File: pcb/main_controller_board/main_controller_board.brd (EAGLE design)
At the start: 72.1 x 52.1 mm, 3 parts, among them U1 RPI_CAMERA, U2 RPI_CAMERA

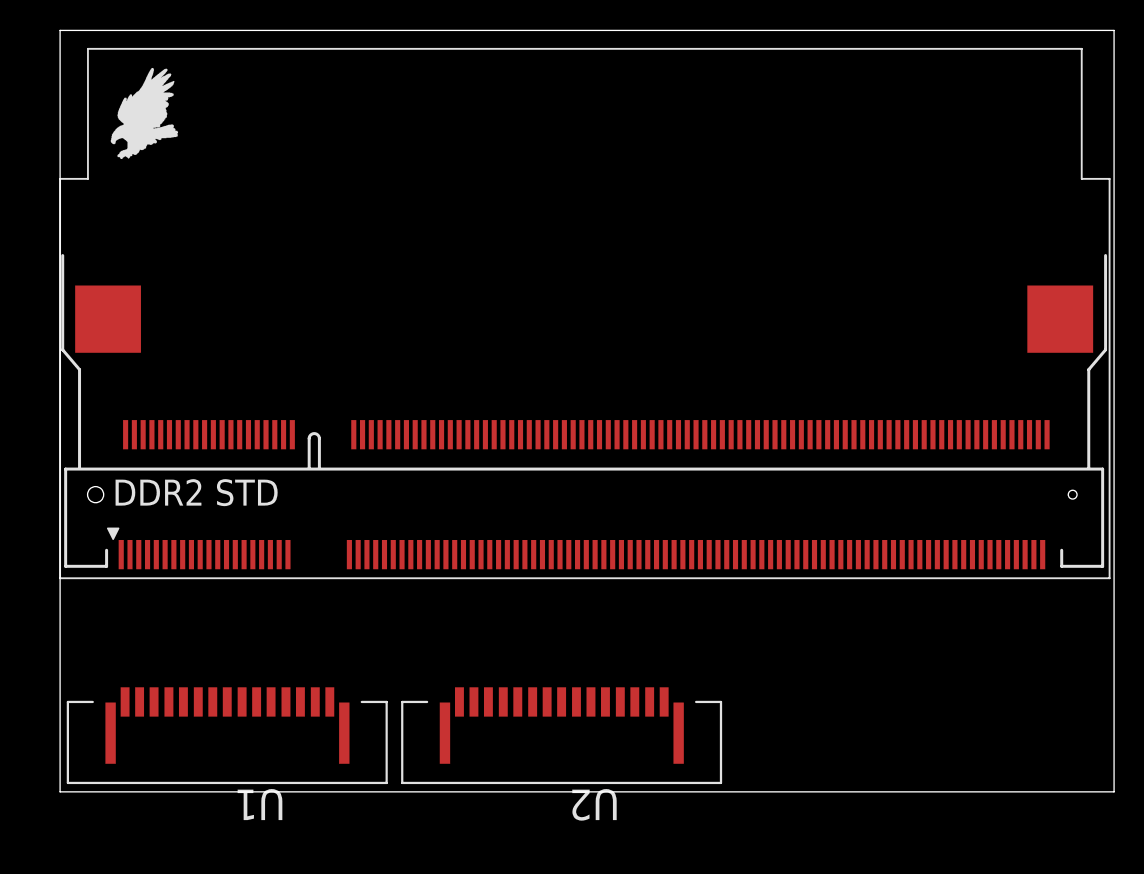
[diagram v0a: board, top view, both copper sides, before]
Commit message: add dc-dc
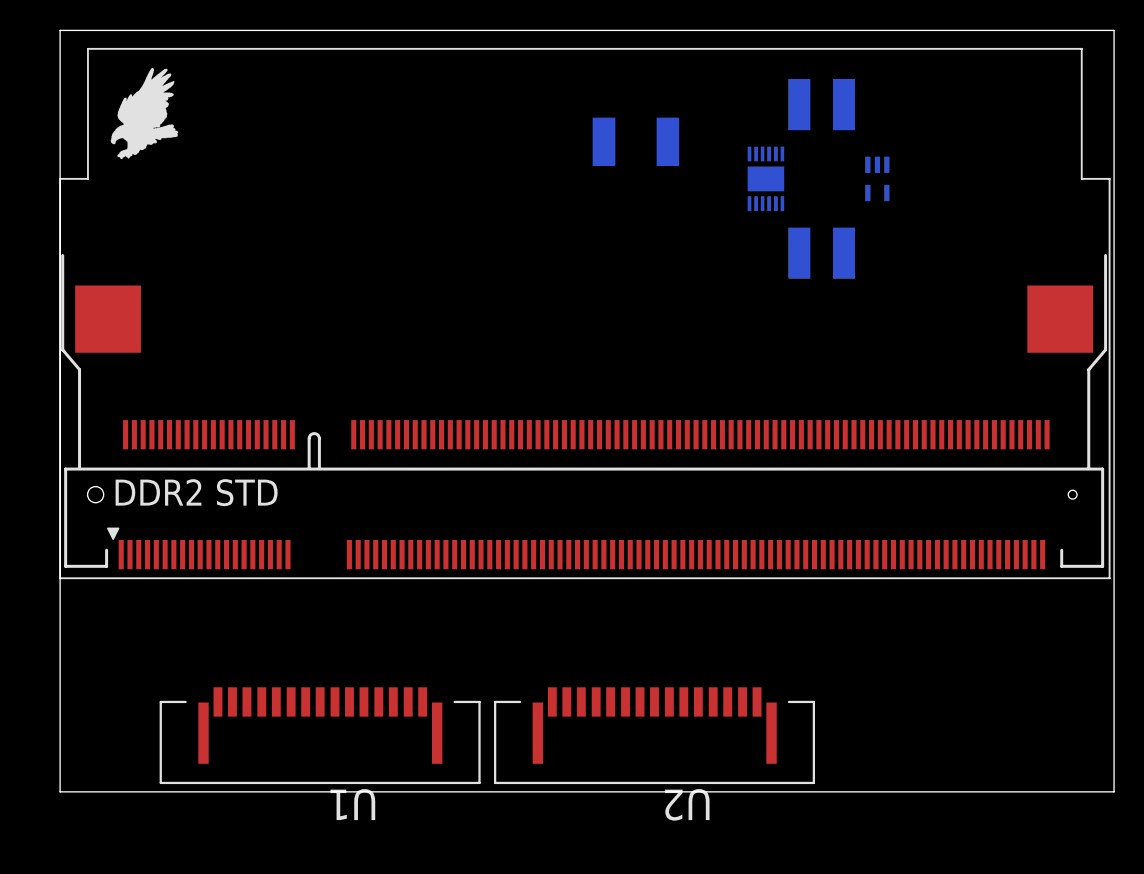
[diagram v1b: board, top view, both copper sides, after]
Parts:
- added F1: (no value), openblw:1812
- added L1, L2: (no value), openblw:BOURNS-SRN4018
- added U$1: PAM2306, openblw:WDFN3X3-12L
- added U$2: AP7115-XXSEG, openblw:SOT353
- moved U1 6.35 mm to (17.8, 8.89)
- moved U2 6.35 mm to (40.6, 8.89)
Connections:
- new net IN: U$2.1

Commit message: porovisional wiring
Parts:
- added C1, C9: 100n, resistor:C0402
- added C10: 4.7u, resistor:C0603
- added C11, C12, C13, C14: (no value), resistor:C1206
- added C2, C3, C6, C7: 10u, resistor:C0805
- added C4, C5: NF, resistor:C0402
- added C8: 1u, resistor:C0402
- added CN1: (no value), openblw:JST-PH-2-THM
- added H1, H2, H3, H4: MOUNT-PAD-ROUND2.8, holes:2,8-PAD
- added IC1: (no value), openblw:DIP_3PIN
- added JP1: (no value), pinhead:1X04
- added K1: 61400416021, openblw:61400416021
- added LED1: RED, led:CHIP-LED0603
- added LED2: GREEN, led:CHIP-LED0603
- added R1, R11, R12: 100K, resistor:R0402
- added R10, R7, R8, R9: 0R, resistor:R0805
- added R13, R14, R16, R17: 1.8K, resistor:R0402
- added R15, R6: 470R, resistor:R0402
- added R2, R3: 0R, resistor:R0402
- added R4, R5: NR, resistor:R0402
- added U$3: DMG1012T, openblw:SOT523
- F1: value (none) -> MF-MSMF110/16
- L1, L2: value (none) -> 4.7u
- moved U$2 44.7 mm to (11.2, 40.6), turned to 0 degrees
- moved L1 35.3 mm to (16.8, 48.0), turned to 180 degrees
- moved U1 30.7 mm to (48.5, 8.26)
- moved U$1 27.5 mm to (20.8, 42.9)
- moved L2 27.2 mm to (24.9, 37.8)
- moved U2 18.9 mm to (21.7, 8.26)
- moved F1 12.8 mm to (52.1, 43.2), flipped to the top, turned to 270 degrees
- moved PCB1 1.42 mm to (36.2, 21.6), flipped to the bottom
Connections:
- removed net IN: U$2.1
- new net +12V: F1.2, IC1.IN
- new net +1V8: C5.1, C7.1, L2.P$1, R3.1, R9.2
- new net +2V5: C10.1, R10.2, U$2.5
- new net +3V3: C4.1, C6.1, C8.1, L1.P$1, R13.2, R14.2, R15.1, R16.2, R17.2, R2.1, R6.1, R7.2, R8.2, U$2.1, U$2.3, U1.15, U2.15
- new net +5V: C11.1, C2.1, C3.1, IC1.OUT, JP1.1, K1.1, R1.1, U$1.1, U$1.6, U$1.7
- new net BOTTOM_LIGHT_ENABLED: PCB1.59
- new net CAM0_CN: PCB1.144, U1.8
- new net CAM0_CP: PCB1.142, U1.9
- new net CAM0_DN0: PCB1.138, U1.2
- new net CAM0_DN1: PCB1.150, U1.5
- new net CAM0_DP0: PCB1.136, U1.3
- new net CAM0_DP1: PCB1.148, U1.6
- new net CAM0_IO0: PCB1.36, U1.11
- new net CAM0_IO1: PCB1.34, U1.12
- new net CAM0_SCL: PCB1.30, R13.1, U1.13
- new net CAM0_SDA: PCB1.28, R14.1, U1.14
- new net CAM1_CN: PCB1.149, U2.8
- new net CAM1_CP: PCB1.147, U2.9
- new net CAM1_DN0: PCB1.161, U2.2
- new net CAM1_DN1: PCB1.155, U2.5
- new net CAM1_DP0: PCB1.159, U2.3
- new net CAM1_DP1: PCB1.153, U2.6
- new net CAM1_IO0: PCB1.11, U2.11
- new net CAM1_IO1: PCB1.9, U2.12
- new net CAM1_SCL: PCB1.5, R17.1, U2.13
- new net CAM1_SDA: PCB1.3, R16.1, U2.14
- new net CM_1V8: C12.1, PCB1.183, PCB1.184, PCB1.185, PCB1.186, R9.1
- new net CM_3V3: C13.1, PCB1.191, PCB1.192, PCB1.193, PCB1.194, R8.1
- new net CM_VBAT: C14.1, PCB1.197, PCB1.198, PCB1.199, PCB1.200, R7.1
- new net CM_VDAC: PCB1.189, PCB1.190, R10.1
- new net EMMC_DISABLE_N: PCB1.2
- new net EXT0: PCB1.63
- new net EXT1: PCB1.65
- new net GND: C1.2, C10.2, C11.2, C12.2, C13.2, C14.2, C2.2, C3.2, C6.2, C7.2, C8.2, C9.2, CN1.2, H1.B2,8, H2.B2,8, H3.B2,8, H4.B2,8, IC1.GND, JP1.4, K1.4, LED1.C, PCB1.1, PCB1.103, PCB1.104, PCB1.109, PCB1.110, PCB1.115, PCB1.121, PCB1.122, PCB1.127, PCB1.13, PCB1.133, PCB1.134, PCB1.139, PCB1.140, PCB1.145, PCB1.146, PCB1.151, PCB1.152, PCB1.157, PCB1.163, PCB1.164, PCB1.169, PCB1.170, PCB1.181, PCB1.182, PCB1.187, PCB1.188, PCB1.19, PCB1.195, PCB1.196, PCB1.25, PCB1.26, PCB1.31, PCB1.32, PCB1.37, PCB1.38, PCB1.43, PCB1.44, PCB1.49, PCB1.50, PCB1.55, PCB1.56, PCB1.61, PCB1.62, PCB1.67, PCB1.68, PCB1.7, PCB1.73, PCB1.74, PCB1.79, PCB1.80, PCB1.85, PCB1.86, PCB1.91, PCB1.92, PCB1.97, PCB1.98, R11.2, R12.2, R4.2, R5.2, U$1.3, U$1.9, U$1.PAD, U$2.2, U$3.2, U1.1, U1.10, U1.4, U1.7, U2.1, U2.10, U2.4, U2.7
- new net GPIO47_1V8: PCB1.90, U$3.1
- new net N$1: C1.1, R1.2, U$1.12
- new net N$10: C5.2, R3.2, R4.1, U$1.10
- new net N$11: PCB1.154
- new net N$12: PCB1.156
- new net N$13: PCB1.158
- new net N$14: PCB1.160
- new net N$15: PCB1.162
- new net N$16: PCB1.10
- new net N$17: PCB1.12
- new net N$18: PCB1.14
- new net N$19: PCB1.16
- new net N$2: L1.P$2, U$1.8
- new net N$20: PCB1.18
- new net N$21: PCB1.20
- new net N$22: PCB1.22
- new net N$23: PCB1.24
- new net N$24: PCB1.124
- new net N$25: PCB1.126
- new net N$26: PCB1.128
- new net N$27: PCB1.130
- new net N$28: PCB1.132
- new net N$29: PCB1.4
- new net N$3: U$1.5
- new net N$30: PCB1.6
- new net N$31: PCB1.82, R12.1
- new net N$32: LED2.A, R15.2
- new net N$33: LED2.C, U$3.3
- new net N$34: PCB1.84, R11.1
- new net N$35: PCB1.8
- new net N$4: U$1.11
- new net N$5: C9.1, U$2.4
- new net N$6: CN1.1, F1.1
- new net N$7: L2.P$2, U$1.2
- new net N$8: C4.2, R2.2, R5.1, U$1.4
- new net N$9: LED1.A, R6.2
- new net TOP_LIGHT_ENABLED: PCB1.57
- new net UART_RX: JP1.3, PCB1.53
- new net UART_TX: JP1.2, PCB1.51
- new net USB_DN: K1.2, PCB1.167
- new net USB_DP: K1.3, PCB1.165
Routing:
- net +3V3: track 0.00 -> 185.0 mm, vias 0 -> 6
- net +5V: track 0.00 -> 72.1 mm, vias 0 -> 2
- net CAM1_SDA: track 0.00 -> 50.6 mm, vias 0 -> 1
- net CAM1_SCL: track 0.00 -> 47.3 mm, vias 0 -> 1
- net CAM1_IO0: track 0.00 -> 47.0 mm, vias 0 -> 1
- net CAM1_IO1: track 0.00 -> 46.8 mm, vias 0 -> 1
- net CAM0_CP: track 0.00 -> 43.5 mm, vias 0 -> 1
- net CAM0_CN: track 0.00 -> 42.7 mm, vias 0 -> 1
- net CAM0_DN1: track 0.00 -> 42.2 mm, vias 0 -> 1
- net CAM0_DP1: track 0.00 -> 42.1 mm, vias 0 -> 1
- net GPIO47_1V8: track 0.00 -> 40.7 mm, vias 0 -> 1
- net USB_DN: track 0.00 -> 36.2 mm, vias 0 -> 1
- net CAM0_DP0: track 0.00 -> 35.8 mm, vias 0 -> 1
- net CAM0_DN0: track 0.00 -> 35.5 mm, vias 0 -> 1
- net USB_DP: track 0.00 -> 35.3 mm, vias 0 -> 1
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- added copper zone on layer 16, net CM_1V8
- added copper zone on layer 16, net CM_3V3
- added copper zone on layer 16, net CM_VBAT
- added copper zone on layer 1, net GND
- added copper zone on layer 16, net GND

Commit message: rev0.1
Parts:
- added U$4: TENDA_P200, openblw:TENDA_P200
- moved JP1 40.1 mm to (22.9, 29.0), turned to 0 degrees
- moved R16 34.0 mm to (34.8, 4.06), flipped to the top, turned to 0 degrees
- moved R17 33.2 mm to (34.8, 2.79), flipped to the top, turned to 0 degrees
- moved C11 30.2 mm to (19.1, 35.6), turned to 180 degrees
- moved F1 27.0 mm to (25.1, 41.4)
- moved R13 26.6 mm to (61.5, 2.79), flipped to the top, turned to 0 degrees
- moved CN1 26.0 mm to (24.9, 46.7)
- moved IC1 25.8 mm to (25.1, 33.0)
- moved R14 25.2 mm to (61.5, 4.06), flipped to the top, turned to 0 degrees
- moved R1 11.3 mm to (16.0, 45.2)
- moved C1 11.1 mm to (14.5, 46.5)
- moved C7 6.75 mm to (20.1, 40.6)
- moved R2 6.75 mm to (14.5, 37.1)
- moved L2 6.75 mm to (18.5, 35.6)
- moved C4 6.67 mm to (14.5, 35.8)
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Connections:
- net CAM0_CN renamed CAM0_C_N
- net CAM0_CP renamed CAM0_C_P
- net CAM0_DN0 renamed CAM0_D0_N
- net CAM0_DN1 renamed CAM0_D1_N
- net CAM0_DP0 renamed CAM0_D0_P
- net CAM0_DP1 renamed CAM0_D1_P
- net CAM1_CN renamed CAM1_C_N
- net CAM1_CP renamed CAM1_C_P
- net CAM1_DN0 renamed CAM1_D0_N
- net CAM1_DN1 renamed CAM1_D1_N
- net CAM1_DP0 renamed CAM1_D0_P
- net CAM1_DP1 renamed CAM1_D1_P
- net USB_DN renamed USB_D_N
- net USB_DP renamed USB_D_P
- new net DGND: U$4.5, U$4.6
- net +12V: now also U$4.1, U$4.2
- net +3V3: now also U$4.7, U$4.8
- net GND: now also U$4.12
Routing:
- net DGND: track 0.00 -> 41.3 mm
- net USB_D_P: track 35.3 -> 61.8 mm
- net USB_D_N: track 36.2 -> 61.1 mm
- net CM_VBAT: track 0.00 -> 22.4 mm, vias 0 -> 1
- net CM_3V3: track 0.48 -> 21.2 mm, vias 0 -> 1
- net CM_1V8: track 0.83 -> 21.3 mm, vias 0 -> 1
- net +5V: track 72.1 -> 55.4 mm
- net CAM1_SCL: track 47.3 -> 58.5 mm, vias 1 -> 3
- net +12V: track 4.16 -> 14.5 mm
- net +3V3: track 185.0 -> 178.7 mm, vias 6 -> 2
- net +1V8: track 34.1 -> 28.6 mm
- net CAM0_D0_N: track 35.5 -> 40.2 mm
- net CAM1_SDA: track 50.6 -> 55.2 mm, vias 1 -> 3
- net CAM0_SCL: track 25.8 -> 30.3 mm, vias 1 -> 3
- net CAM0_D0_P: track 35.8 -> 40.2 mm
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- added copper zone on layer 16, net +5V
- removed copper zone on layer 16, net CM_1V8
- removed copper zone on layer 16, net CM_3V3
- removed copper zone on layer 16, net CM_VBAT
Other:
- board size 72.1 x 52.1 mm -> 72 x 50 mm

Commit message: before export gerber
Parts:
- added C15: 10u, resistor:C1206
- C11: value (none) -> 22u
- PCB1: value RPI_COMPUTE -> RPCM
- U1: value RPI_CAMERA -> CAMERA0
- U2: value RPI_CAMERA -> CAMERA1
- moved IC1 3.42 mm to (27.4, 35.6), turned to 270 degrees
- moved C11 3.12 mm to (20.9, 33.0)
- moved F1 1.38 mm to (24.1, 42.2), turned to 180 degrees
- renumbered U$1 to U5, U$2 to U6, U$3 to U3, U$4 to U4
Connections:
- net DGND renamed PLC_N
- new net PLC_P: U4.1, U4.2
- net +12V: now also C15.1; no longer U4.1, U4.2
- net GND: now also C15.2
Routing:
- net GND: track 0.00 -> 24.2 mm, vias 169 -> 167
- net PLC_P: track 0.00 -> 20.5 mm
- net +3V3: track 178.7 -> 160.9 mm, vias 2 -> 5
- net +5V: track 55.4 -> 64.2 mm, vias 2 -> 3
- net +12V: track 14.5 -> 8.01 mm
- net PLC_N: track 41.3 -> 35.4 mm
- net +1V8: track 28.6 -> 26.8 mm, vias 0 -> 2
- net N$6: track 3.44 -> 4.63 mm
- added copper zone on layer 15, net GND
- added copper zone on layer 2, net GND

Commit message: before order 0
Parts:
- added LOGO1: (no value), openblw:OHMYDIGIFAB_LOGO
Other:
- outline, holes or cut-outs redrawn
- board text added: "MainController"
- board text added: "OpenBLW"
- board text added: "Rev.0.1"
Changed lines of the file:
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@@
 <board limitedwidth="160">
 <plain>
-<wire x1="0" y1="0" x2="68.4" y2="0" width="0" layer="20"/>
-<wire x1="68.4" y1="0" x2="72" y2="0" width="0" layer="20"/>
-<wire x1="72" y1="0" x2="72" y2="46.4" width="0" layer="20"/>
-<wire x1="72" y1="46.4" x2="72" y2="50" width="0" layer="20"/>
-<wire x1="72" y1="50" x2="3.6" y2="50" width="0" layer="20"/>
-<wire x1="3.6" y1="50" x2="0" y2="50" width="0" layer="20"/>
-<wire x1="0" y1="50" x2="0" y2="3.6" width="0" layer="20"/>
-<wire x1="0" y1="3.6" x2="0" y2="0" width="0" layer="20"/>
-<wire x1="0" y1="3.6" x2="3.6" y2="0" width="0.254" layer="20" curve="90"/>
-<wire x1="3.6" y1="0" x2="68.4" y2="0" width="0.254" layer="20"/>
-<wire x1="68.4" y1="0" x2="72" y2="3.6" width="0.254" layer="20" curve="90"/>
-<wire x1="72" y1="3.6" x2="72" y2="46.4" width="0.254" layer="20"/>
-<wire x1="72" y1="46.4" x2="68.4" y2="50" width="0.254" layer="20" curve="90"/>
-<wire x1="68.4" y1="50" x2="3.6" y2="50" width="0.254" layer="20"/>
-<wire x1="3.6" y1="50" x2="0" y2="46.4" width="0.254" layer="20" curve="90"/>
-<wire x1="0" y1="46.4" x2="0" y2="3.6" width="0.254" layer="20"/>
+<wire x1="0" y1="3.6" x2="3.6" y2="0" width="0" layer="20" curve="90"/>
+<wire x1="3.6" y1="0" x2="68.4" y2="0" width="0" layer="20"/>
+<wire x1="68.4" y1="0" x2="72" y2="3.6" width="0" layer="20" curve="90"/>
+<wire x1="72" y1="3.6" x2="72" y2="46.4" width="0" layer="20"/>
+<wire x1="72" y1="46.4" x2="68.4" y2="50" width="0" layer="20" curve="90"/>
+<wire x1="68.4" y1="50" x2="3.6" y2="50" width="0" layer="20"/>
+<wire x1="3.6" y1="50" x2="0" y2="46.4" width="0" layer="20" curve="90"/>
+<wire x1="0" y1="46.4" x2="0" y2="3.6" width="0" layer="20"/>
+<text x="46.99" y="44.958" size="2.54" layer="21">OpenBLW</text>
+<text x="49.53" y="41.148" size="1.778" layer="21">MainController</text>
+<text x="57.404" y="38.354" size="1.778" layer="21">Rev.0.1</text>
 </plain>
 <attributes>
@@
 <element name="H4" library="holes" package="2,8-PAD" value="MOUNT-PAD-ROUND2.8" x="3.6" y="46.4" smashed="yes"/>
 <element name="U4" library="openblw" package="TENDA_P200" value="TENDA_P200" x="30.734" y="32.512" smashed="yes" rot="R270">
-<attribute name="NAME" x="66.929" y="12.192" size="1.016" layer="25" ratio="10" rot="R270"/>
+<attribute name="NAME" x="60.96" y="5.969" size="1.016" layer="25" ratio="10"/>
 <attribute name="VALUE" x="28.829" y="32.512" size="1.016" layer="27" rot="R270"/>
 </element>
@@
 <attribute name="VALUE" x="21.3868" y="40.132" size="0.6096" layer="27" rot="R180"/>
 </element>
+<element name="LOGO1" library="openblw" package="OHMYDIGIFAB_LOGO" value="" x="68.326" y="9.144"/>
 </elements>
 <signals>

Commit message: 0.5mm clearance
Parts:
- C11, C15: device resistor:C1206 -> resistor:153CLV-0405
- C12, C13, C14: value (none) -> 47u
- moved C15 1.37 mm to (19.5, 38.1), turned to 0 degrees
- moved C11 1.35 mm to (19.5, 33.0), turned to 0 degrees
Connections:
- net +12V: now also C15.+; no longer C15.1
- net +5V: now also C11.+; no longer C11.1
- net GND: now also C11.-, C15.-; no longer C11.2, C15.2
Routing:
- net +5V: track 64.2 -> 66.8 mm
- net +12V: track 8.01 -> 8.98 mm

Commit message: order
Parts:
- CN1: value (none) -> B2B-PH-K-S
- F1: value MF-MSMF110/16 -> MF-MSMF200
- IC1: value (none) -> V7805-1000
- JP1: value (none) -> 90131-0764; device pinhead:1X04 -> pinhead:2X04
- PCB1: value RPCM -> 1473005-4
- U1: value CAMERA0 -> SFW15R-1STE1LF
- U2: value CAMERA1 -> SFW15R-1STE1LF
- U5: value PAM2306 -> PAM2306AYPKE
- U6: value AP7115-XXSEG -> AP7115-25SEG
- moved H3 2.15 mm to (66.2, 46.4)
- moved H4 1.90 mm to (5.50, 46.4)
- moved JP1 0.57 mm to (22.4, 28.7)
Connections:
- removed net EXT0: PCB1.63
- removed net EXT1: PCB1.65
- removed net UART_RX: JP1.3, PCB1.53
- removed net UART_TX: JP1.2, PCB1.51
- new net EXT0/UART1_TX: JP1.6, PCB1.70
- new net EXT1/UART1_RX: JP1.4, PCB1.72
- new net UART0_RX: JP1.5, PCB1.53
- new net UART0_TX: JP1.3, PCB1.51
- net +5V: now also JP1.2
- net GND: now also JP1.7, JP1.8; no longer JP1.4
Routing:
- net UART0_RX: track 0.00 -> 34.1 mm, vias 0 -> 1
- net UART_RX: track 33.1 -> 0.00 mm, vias 1 -> 0
- net UART0_TX: track 0.00 -> 32.1 mm, vias 0 -> 1
- net UART_TX: track 31.2 -> 0.00 mm, vias 1 -> 0
- net EXT0/UART1_TX: track 0.00 -> 29.3 mm, vias 0 -> 1
- net EXT1/UART1_RX: track 0.00 -> 25.5 mm, vias 0 -> 1
- net USB_D_P: track 61.8 -> 59.7 mm
- net USB_D_N: track 61.1 -> 59.0 mm
- net +5V: track 66.8 -> 68.4 mm
- net GND: vias 167 -> 169

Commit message: lmcl_board
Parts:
- added C16: 1u, resistor:C0402
- added C17: 10n, resistor:C0402
- added FB1: MI0805K601R-10, openblw:R0805
- added L3: 10u, openblw:BOURNS-SRN4018
- added R18: 1K, resistor:R0402
- moved LOGO1 30.5 mm to (66.3, 39.6)
- moved IC1 5.36 mm to (24.6, 31.0), turned to 180 degrees
- moved C11 3.70 mm to (16.0, 34.0)
- moved C15 3.59 mm to (16.0, 38.6)
- moved F1 3.29 mm to (24.8, 39.0), turned to 270 degrees
- moved CN1 1.02 mm to (23.9, 46.7)
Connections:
- new net N$36: CN1.1, FB1.1
- new net N$37: C16.1, F1.1, L3.P$1
- new net N$38: C17.1, R18.2
- net GND: now also C16.2, C17.2
- net N$6: now also FB1.2, L3.P$2, R18.1; no longer CN1.1, F1.1
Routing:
- net PLC_P: track 20.5 -> 28.1 mm
- net N$37: track 0.00 -> 6.62 mm
- net USB_D_N: track 59.0 -> 54.0 mm
- net USB_D_P: track 59.7 -> 55.0 mm
- net +1V8: track 27.3 -> 31.4 mm, vias 2 -> 3
- net N$36: track 0.00 -> 3.70 mm
- net +12V: track 8.98 -> 12.1 mm
- net N$38: track 0.00 -> 1.86 mm
- net N$1: track 8.02 -> 9.55 mm
- net N$6: track 4.63 -> 6.13 mm
- net +5V: track 68.4 -> 67.0 mm
- net UART0_RX: track 34.1 -> 33.0 mm
- net GND: track 24.2 -> 25.3 mm, vias 169 -> 165
- net PLC_N: track 35.4 -> 36.5 mm
- net GPIO47_1V8: track 42.8 -> 43.6 mm
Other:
- board text added: "CAM0"
- board text added: "CAM1"
- board text added: "Rev.0.2"
- board text removed: "Rev.0.1"
